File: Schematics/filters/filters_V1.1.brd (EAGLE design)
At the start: 100.6 x 47.9 mm, 110 parts, among them IC1 NE5532N, IC2 NE5532N, IC3 NE5532N, IC4 NE5532N, IC5 NE5532N, IC6 NE5532N, IC7 NE5532N, J1 3_PIN_AMPCONN, J2 3_PIN_AMPCONN, J3 3_PIN_AMPCONN

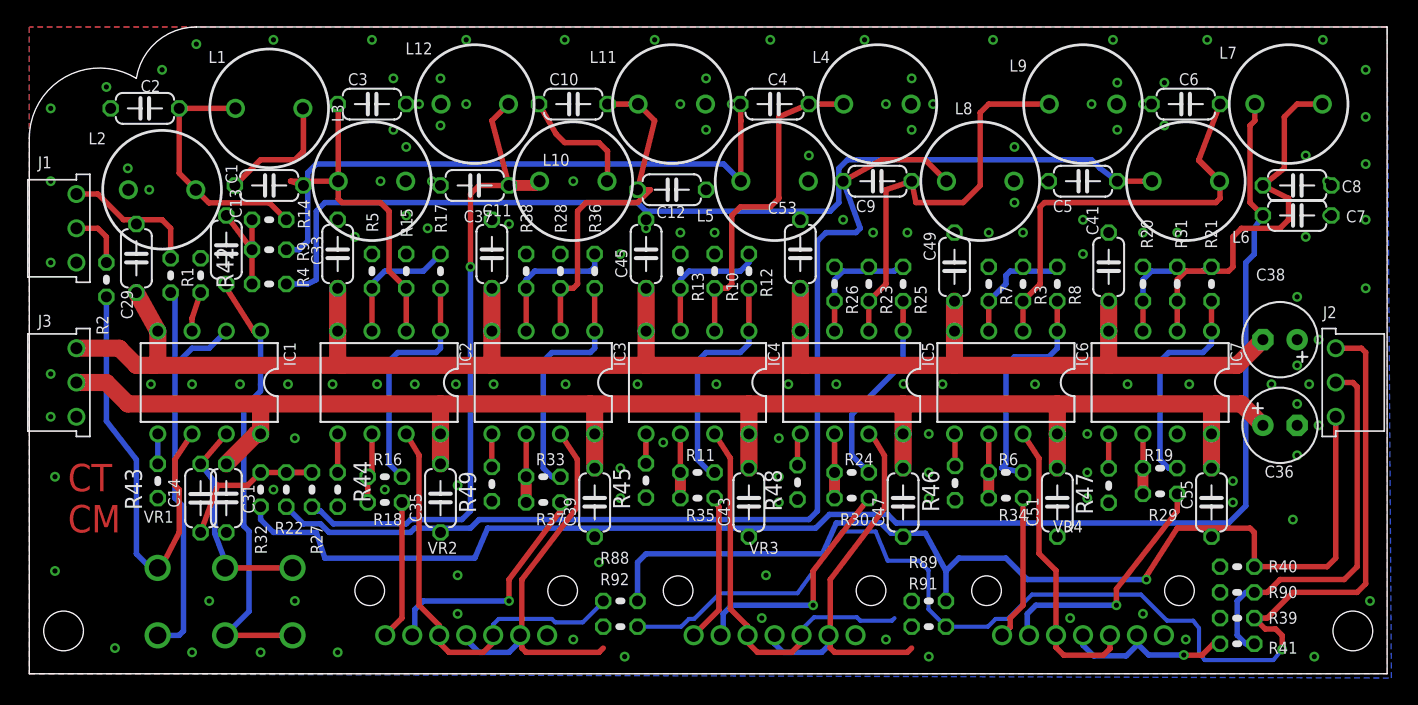
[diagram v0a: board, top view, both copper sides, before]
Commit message: cleaned up filters directory and fixed traces on filter board
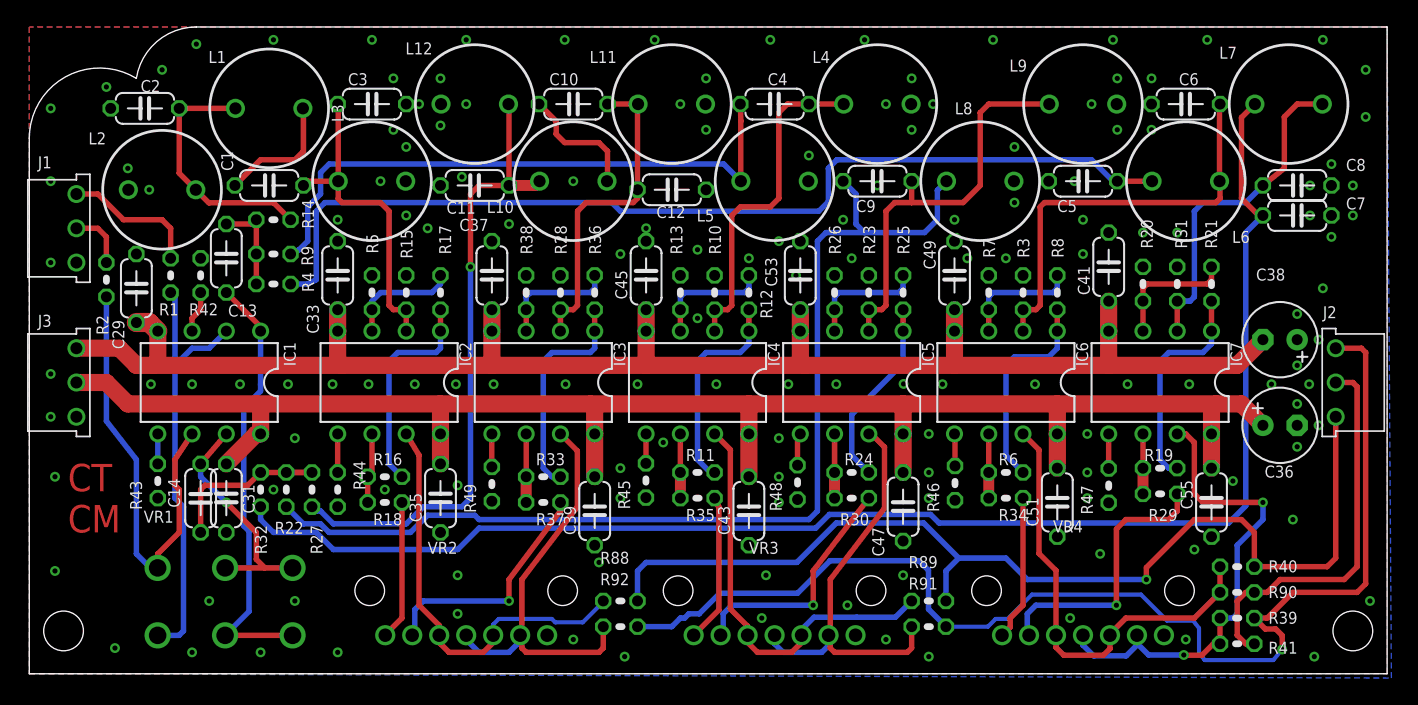
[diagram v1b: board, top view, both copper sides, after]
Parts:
- moved C29 2.22 mm to (7.94, 28.6)
- moved C33 1.59 mm to (22.9, 29.5)
- moved C37 1.59 mm to (34.3, 29.5)
- moved C45 1.59 mm to (45.7, 29.5)
- moved C53 1.59 mm to (57.1, 29.5)
- moved R10 1.59 mm to (50.8, 28.3)
- moved R12 1.59 mm to (53.3, 28.3)
- moved R13 1.59 mm to (48.3, 28.3)
- moved R15 1.59 mm to (27.9, 28.3)
- moved R17 1.59 mm to (30.5, 28.3)
- moved R28 1.59 mm to (39.4, 28.3)
- moved R36 1.59 mm to (41.9, 28.3)
- moved R38 1.59 mm to (36.8, 28.3)
- moved R5 1.59 mm to (25.4, 28.3)
- moved C13 0.64 mm to (14.6, 30.8)
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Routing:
- net N$40: track 13.0 -> 36.1 mm, vias 1 -> 2
- net MVO: track 22.1 -> 33.7 mm
- net -12V: track 127.9 -> 119.4 mm
- net N$14: track 28.0 -> 24.9 mm
- net N$38: track 93.3 -> 90.5 mm
- net N$7: track 33.5 -> 30.9 mm
- net N$59: track 26.3 -> 24.1 mm
- net N$37: track 18.3 -> 20.5 mm
- net N$5: track 16.1 -> 18.1 mm, vias 0 -> 1
- net N$50: track 29.6 -> 31.3 mm
- net N$55: track 29.3 -> 31.1 mm
- net N$41: track 30.1 -> 31.9 mm
- net N$17: track 17.4 -> 15.8 mm
- net N$47: track 18.1 -> 16.5 mm
- net N$15: track 17.6 -> 16.0 mm
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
